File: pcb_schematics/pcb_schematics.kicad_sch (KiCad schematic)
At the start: 71 parts, among them J1 CUE_SJ1-352XNG, J2 Conn_01x01_Pin, J3 Conn_01x05, J4 Conn_01x05, J5 Conn_01x05, SW1 SW_Push, U1 RPi_Pico_TH, U2 RDA5807M_Module, U3 LM386, U4 LM386

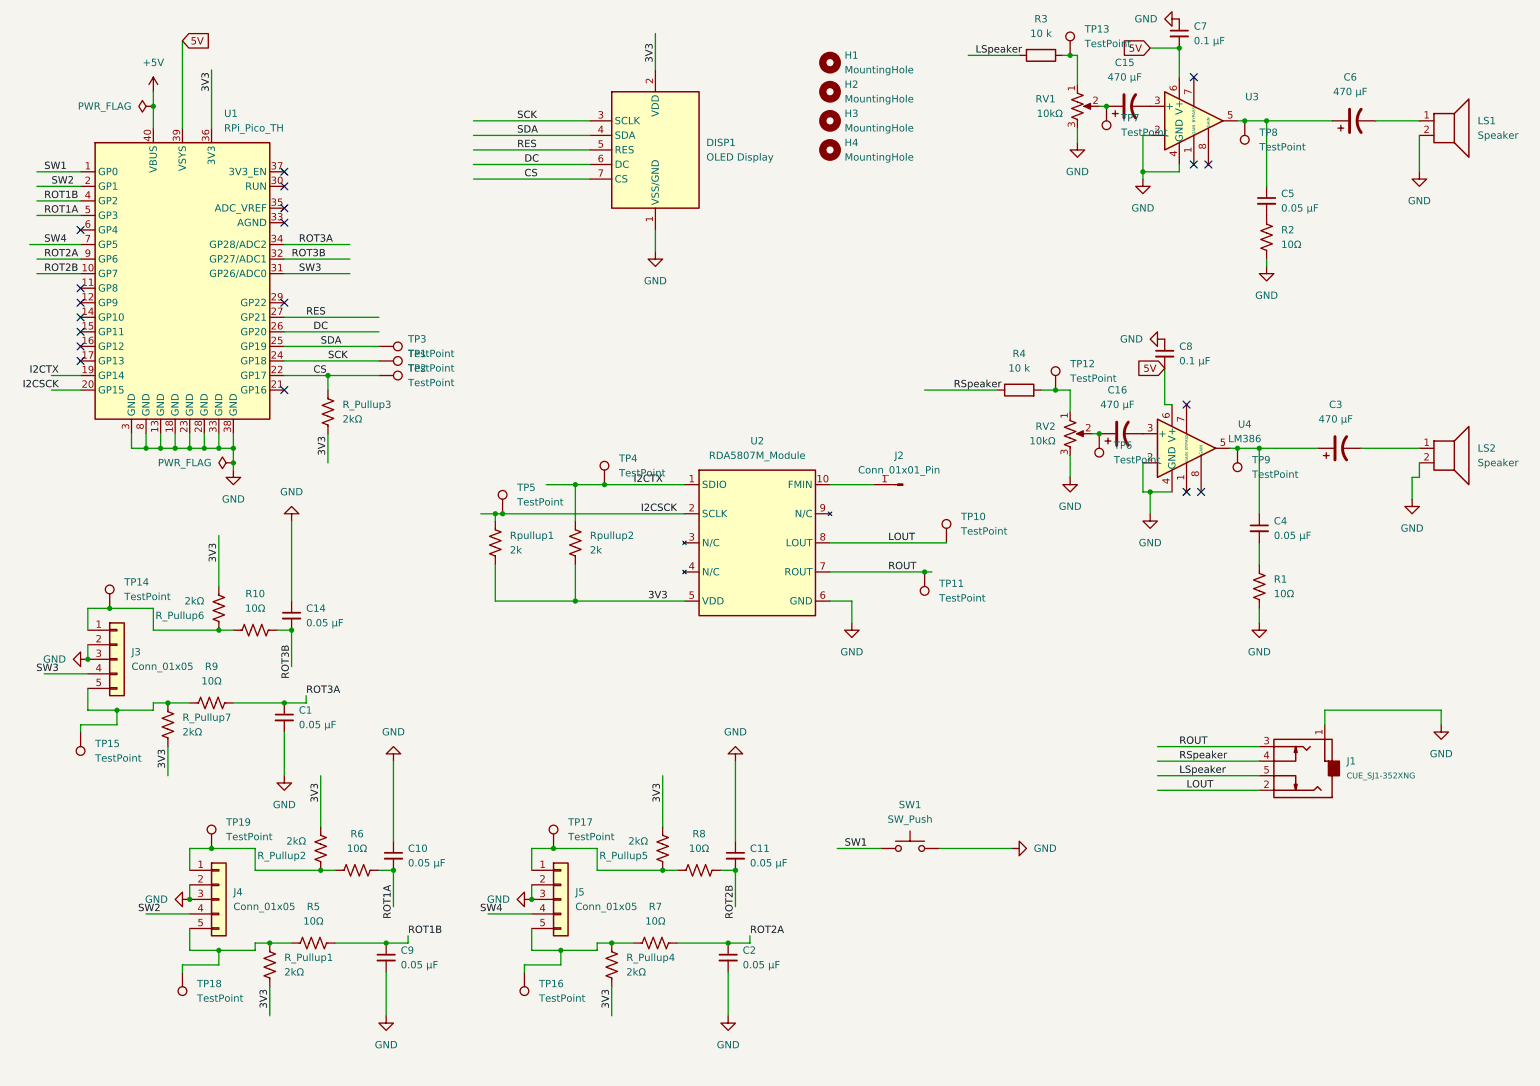
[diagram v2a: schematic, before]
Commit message: fixed issues mentioned by rob and brent
Fix iteration 1
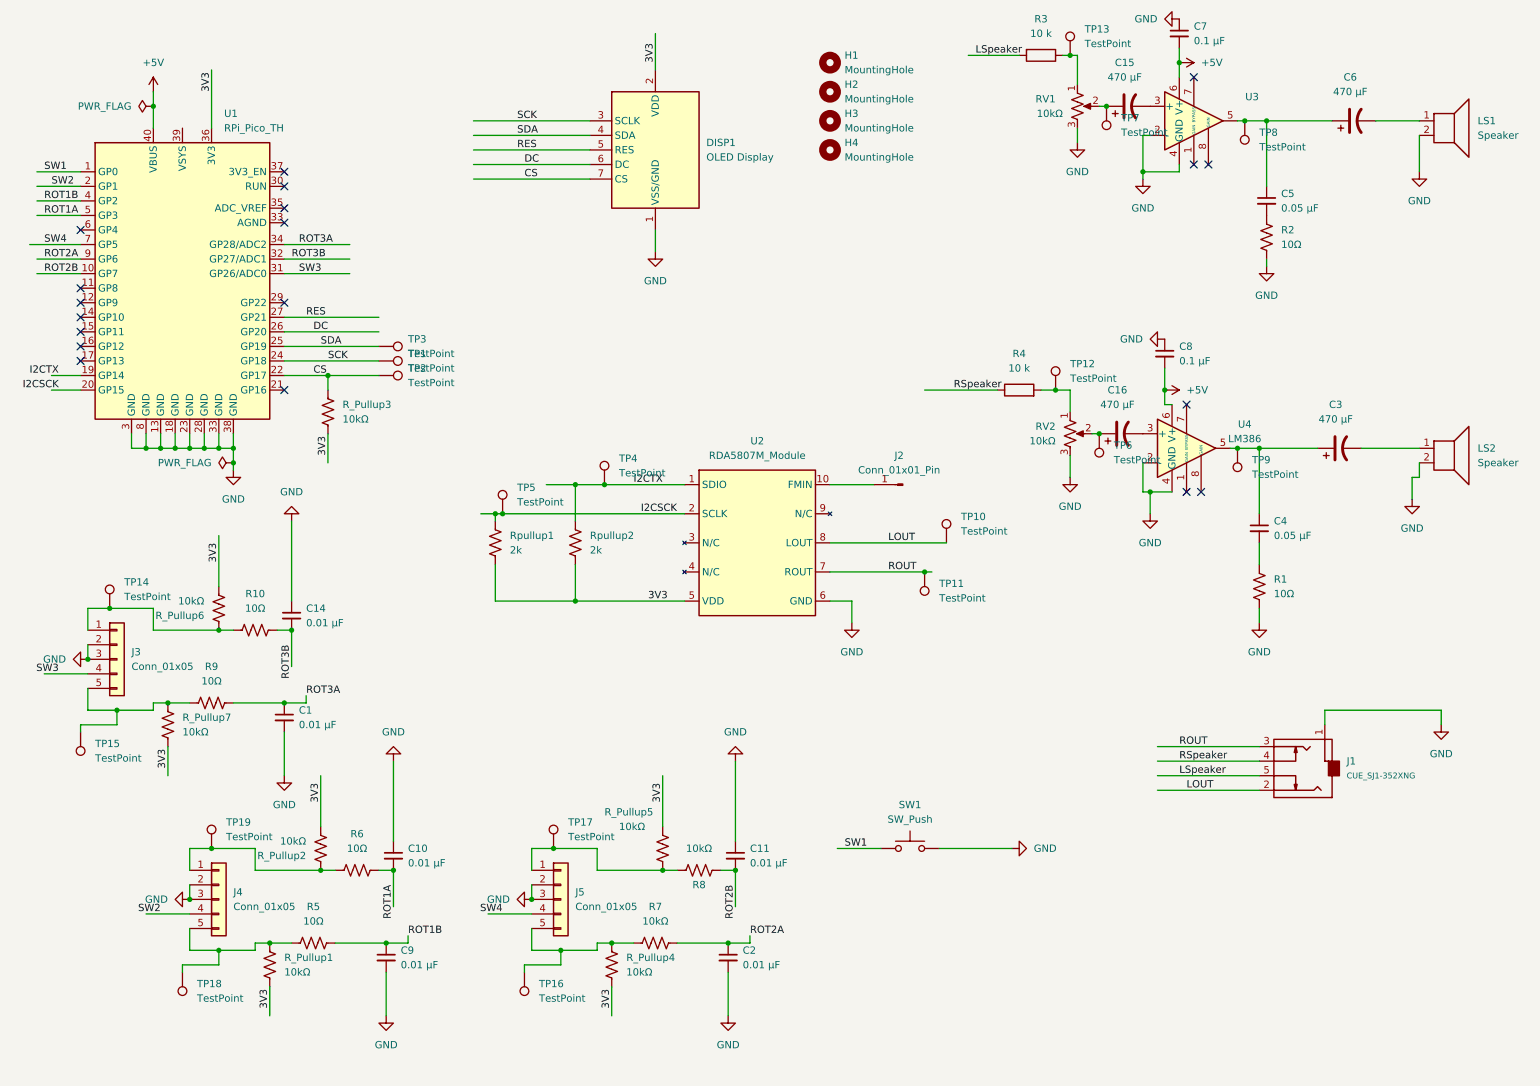
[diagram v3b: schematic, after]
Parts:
- C1, C10, C11, C14, C2, C9: value 0.05 µF -> 0.01 µF
- J3, J4, J5: footprint Connector_PinHeader_2.00mm:PinHeader_1x05_P2.00mm_Vertical -> Connector_PinHeader_2.54mm:PinHeader_1x05_P2.54mm_Vertical
- R7, R8: value 10Ω -> 10kΩ
- R_Pullup1, R_Pullup2, R_Pullup3, R_Pullup4, R_Pullup5, R_Pullup6, R_Pullup7: value 2kΩ -> 10kΩ
- SW1: footprint Connector_PinHeader_1.27mm:PinHeader_1x02_P1.27mm_Vertical -> Connector_PinHeader_2.54mm:PinHeader_1x02_P2.54mm_Vertical
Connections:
- net +5V: now also C7.2, C8.2, U3.6 (V+), U4.6 (V+)
- removed net 5V: C7.2, C8.2, U1.39 (VSYS), U3.6 (V+), U4.6 (V+)

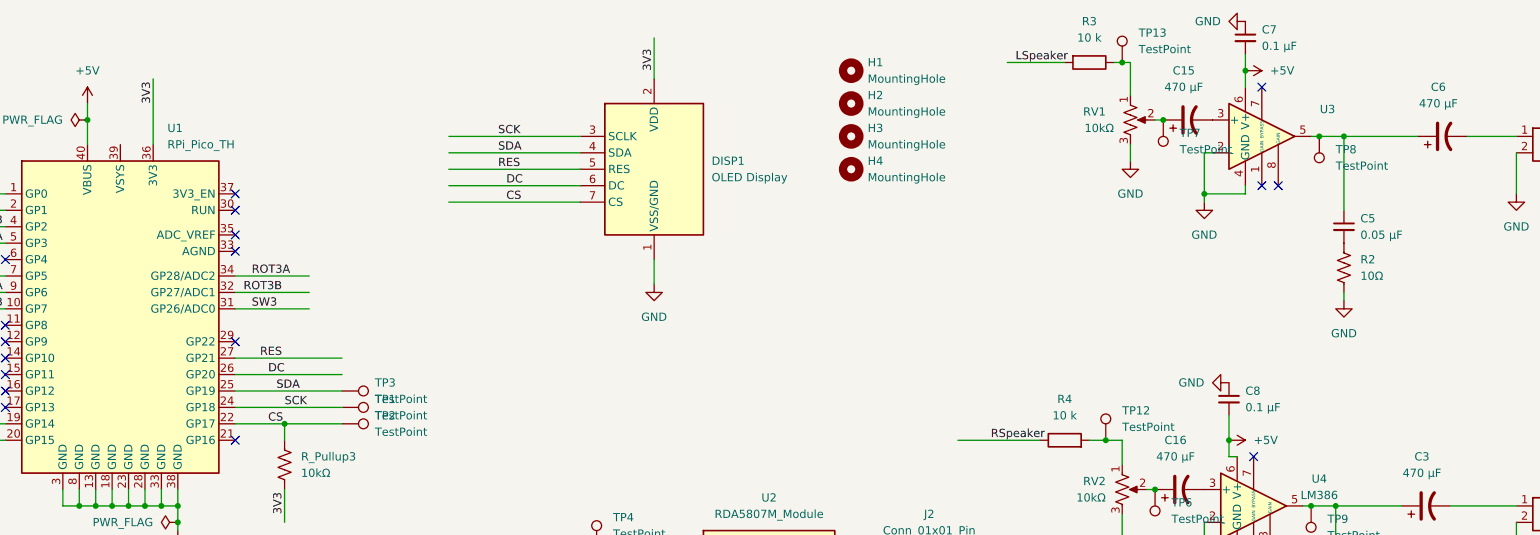
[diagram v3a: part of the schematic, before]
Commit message: made changes based on changes requested
Fix iteration 2
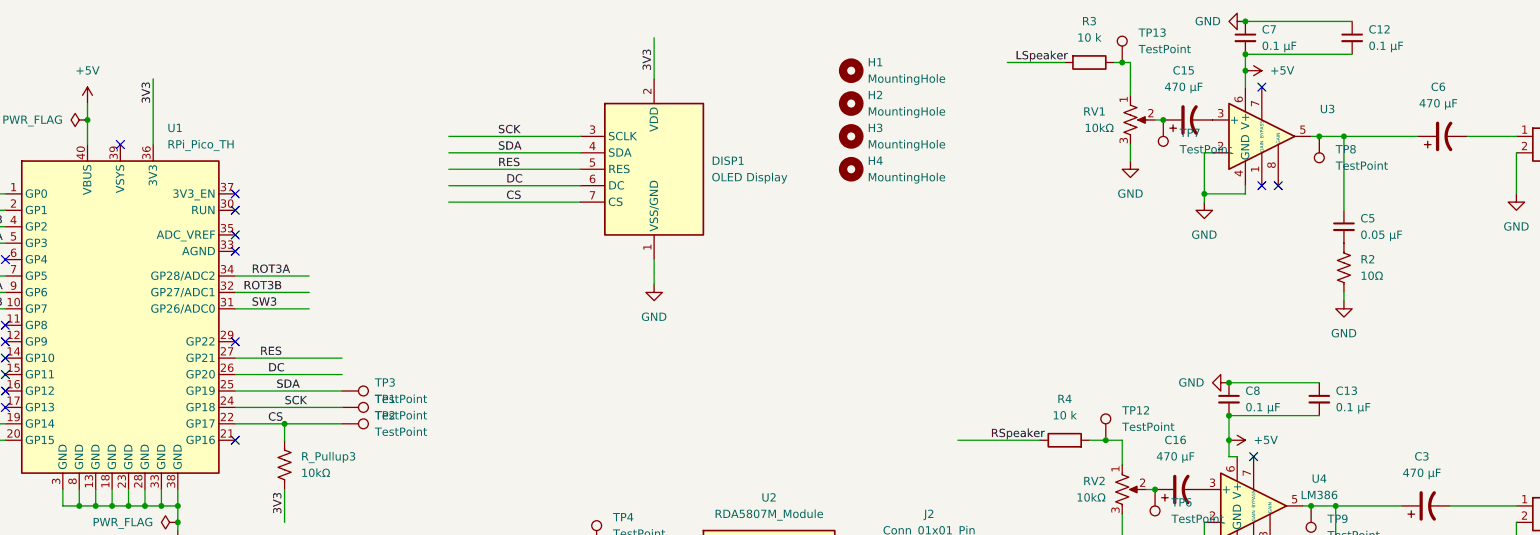
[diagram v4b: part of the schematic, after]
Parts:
- added C12, C13: 0.1 µF, Capacitor_THT:C_Axial_L3.8mm_D2.6mm_P7.50mm_Horizontal, symbol Device:C_Small
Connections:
- net +5V: now also C12.2, C13.2
- net GND: now also C12.1, C13.1
- no-connect marks 19 -> 20
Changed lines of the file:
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@@
   (junction (at 114.3 95.25) (diameter 0) (color 0 0 0 0)
   )
+  (junction (at 217.17 74.93) (diameter 0) (color 0 0 0 0)
+  )
+  (junction (at 217.17 69.85) (diameter 0) (color 0 0 0 0)
+  )
   (junction (at 41.91 88.9) (diameter 0) (color 0 0 0 0)
   )
@@
   (junction (at 40.64 29.21) (diameter 0) (color 0 0 0 0)
   )
+  (junction (at 219.71 13.97) (diameter 0) (color 0 0 0 0)
+  )
   (junction (at 33.02 116.84) (diameter 0) (color 0 0 0 0)
   )
@@
   )
   (junction (at 34.29 134.62) (diameter 0) (color 0 0 0 0)
+  )
+  (junction (at 219.71 19.05) (diameter 0) (color 0 0 0 0)
   )
   (junction (at 71.12 76.2) (diameter 0) (color 0 0 0 0)
@@
   (no_connect (at 63.5 78.74))
   (no_connect (at 222.25 24.13))
+  (no_connect (at 45.72 33.02))
   (no_connect (at 223.52 96.52))
   (no_connect (at 27.94 68.58))
@@
     (stroke (width 0) (type default))
   )
+  (wire (pts (xy 219.71 19.05) (xy 236.22 19.05))
+    (stroke (width 0) (type default))
+  )
   (wire (pts (xy 140.97 180.34) (xy 140.97 187.96))
     (stroke (width 0) (type default))
@@
     (stroke (width 0) (type default))
   )
+  (wire (pts (xy 219.71 13.97) (xy 236.22 13.97))
+    (stroke (width 0) (type default))
+  )
   (wire (pts (xy 39.37 170.18) (xy 46.99 170.18))
     (stroke (width 0) (type default))
@@
     (stroke (width 0) (type default))
   )
+  (wire (pts (xy 217.17 74.93) (xy 231.14 74.93))
+    (stroke (width 0) (type default))
+  )
   (wire (pts (xy 52.07 120.65) (xy 54.61 120.65))
     (stroke (width 0) (type default))
@@
   )
   (wire (pts (xy 215.9 143.51) (xy 233.68 143.51))
+    (stroke (width 0) (type default))
+  )
+  (wire (pts (xy 217.17 69.85) (xy 231.14 69.85))
     (stroke (width 0) (type default))
   )
@@
         (path "/a6913523-cf8b-4e29-b403-fe0fb62af3ee"
           (reference "C6") (unit 1)
+        )
+      )
+    )
+  )
+  (symbol (lib_id "Device:C_Small") (at 231.14 72.39 0) (unit 1)
+    (in_bom yes) (on_board yes) (dnp no) (fields_autoplaced)
+    (property "Reference" "C13" (at 233.68 71.1263 0)
+      (effects (font (size 1.27 1.27)) (justify left))
+    )
+    (property "Value" "0.1 µF" (at 233.68 73.6663 0)
+      (effects (font (size 1.27 1.27)) (justify left))
+    )
+    (property "Footprint" "Capacitor_THT:C_Axial_L3.8mm_D2.6mm_P7.50mm_Horizontal" (at 231.14 72.39 0)
+      (effects (font (size 1.27 1.27)) hide)
+    )
+    (property "Datasheet" "~" (at 231.14 72.39 0)
+      (effects (font (size 1.27 1.27)) hide)
+    )
+    (pin "2")
+    (pin "1")
+    (instances
+      (project "pcb_schematics"
+        (path "/a6913523-cf8b-4e29-b403-fe0fb62af3ee"
+          (reference "C13") (unit 1)
         )
       )
@@
         )
       )
+    )
+  )
+  (symbol (lib_id "Device:C_Small") (at 236.22 16.51 0) (unit 1)
+    (in_bom yes) (on_board yes) (dnp no) (fields_autoplaced)
+    (property "Reference" "C12" (at 238.76 15.2463 0)
+      (effects (font (size 1.27 1.27)) (justify left))
+    )
+    (property "Value" "0.1 µF" (at 238.76 17.7863 0)
+      (effects (font (size 1.27 1.27)) (justify left))
+    )
+    (property "Footprint" "Capacitor_THT:C_Axial_L3.8mm_D2.6mm_P7.50mm_Horizontal" (at 236.22 16.51 0)
+      (effects (font (size 1.27 1.27)) hide)
+    )
+    (property "Datasheet" "~" (at 236.22 16.51 0)
+      (effects (font (size 1.27 1.27)) hide)
+    )
+    (pin "2")
+    (pin "1")
+    (instances
+      (project "pcb_schematics"
+        (path "/a6913523-cf8b-4e29-b403-fe0fb62af3ee"
+          (reference "C12") (unit 1)
+        )
+      )

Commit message: Submitted to JLCPCB
Modification with pcb_schematics being the final version.
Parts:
- J1: footprint ECE:CUE_SJ1-352XNG -> Connector_PinHeader_2.54mm:PinHeader_1x05_P2.54mm_Vertical
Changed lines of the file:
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@@
       (effects (font (size 1.016 1.016)) (justify right))
     )
-    (property "Footprint" "ECE:CUE_SJ1-352XNG" (at 234.95 147.32 0)
+    (property "Footprint" "Connector_PinHeader_2.54mm:PinHeader_1x05_P2.54mm_Vertical" (at 234.95 147.32 0)
       (effects (font (size 1.27 1.27)) hide)
     )
